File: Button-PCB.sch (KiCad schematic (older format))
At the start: 28 parts

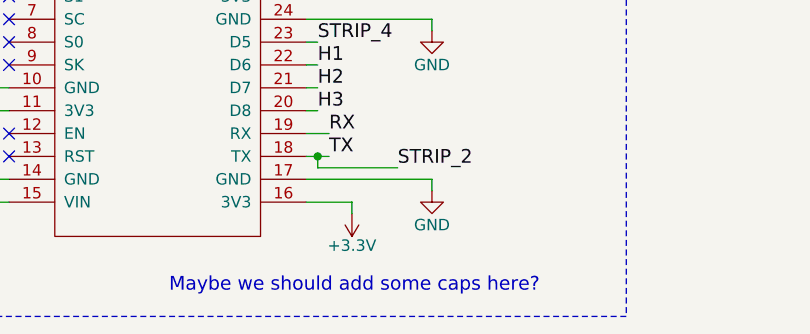
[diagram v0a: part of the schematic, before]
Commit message: Removing note on caps for the nodemcu
Caps are probably not required across the rails of the nodemcu because:

1. The capacitor at the output of the regulator takes care of some
   decoupling already.
2. There's probably a sufficient amount of capacitance on the nodemcu
   board already.
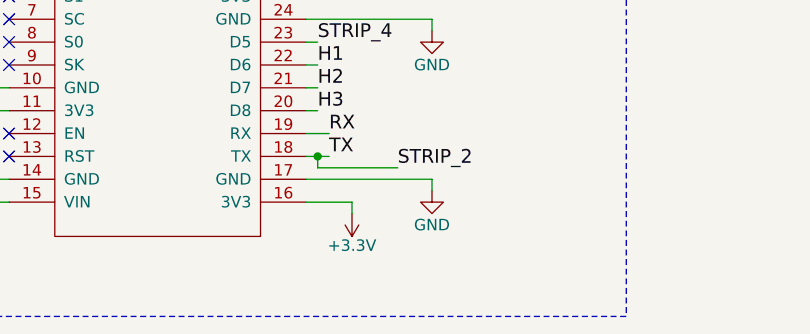
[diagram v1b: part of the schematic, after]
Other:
- note removed: "Maybe we should add some caps here?"
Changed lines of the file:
@@
 LIBS:nodemcuv3
 LIBS:Button-PCB-cache
-EELAYER 25 0
+EELAYER 26 0
 EELAYER END
 $Descr A4 11693 8268
@@
 Wire Wire Line
 	2400 1550 2400 1650
-Text Notes 2900 7000 0    60   ~ 0
-Maybe we should add some caps here?
 Text Notes 600  650  0    60   ~ 0
 Power Input Circuit

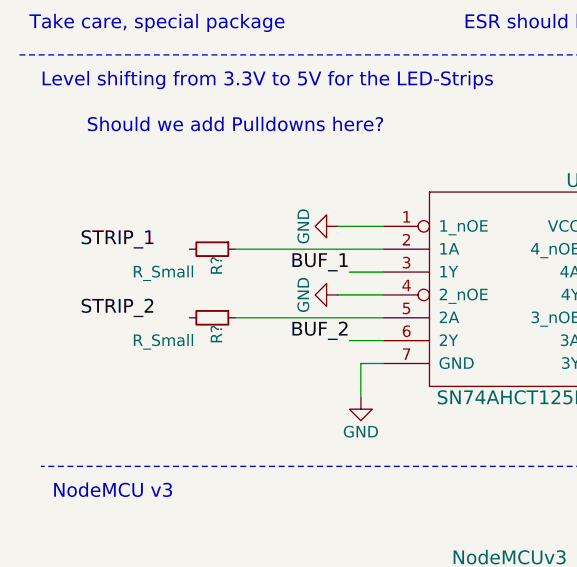
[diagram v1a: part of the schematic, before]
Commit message: Adding missing wire between STRIP label and termination resistors.
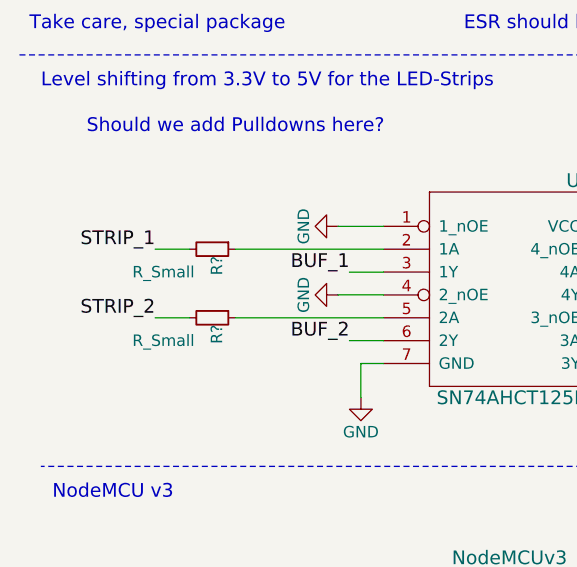
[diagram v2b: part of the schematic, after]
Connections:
- net STRIP_1: now also R?.2
- net STRIP_2: now also R?.2
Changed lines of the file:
@@
 Text Notes 800  3150 0    60   ~ 0
 Should we add Pulldowns here?
+Wire Wire Line
+	1250 3650 1100 3650
+Wire Wire Line
+	1250 3950 1100 3950
 $EndSCHEMATC

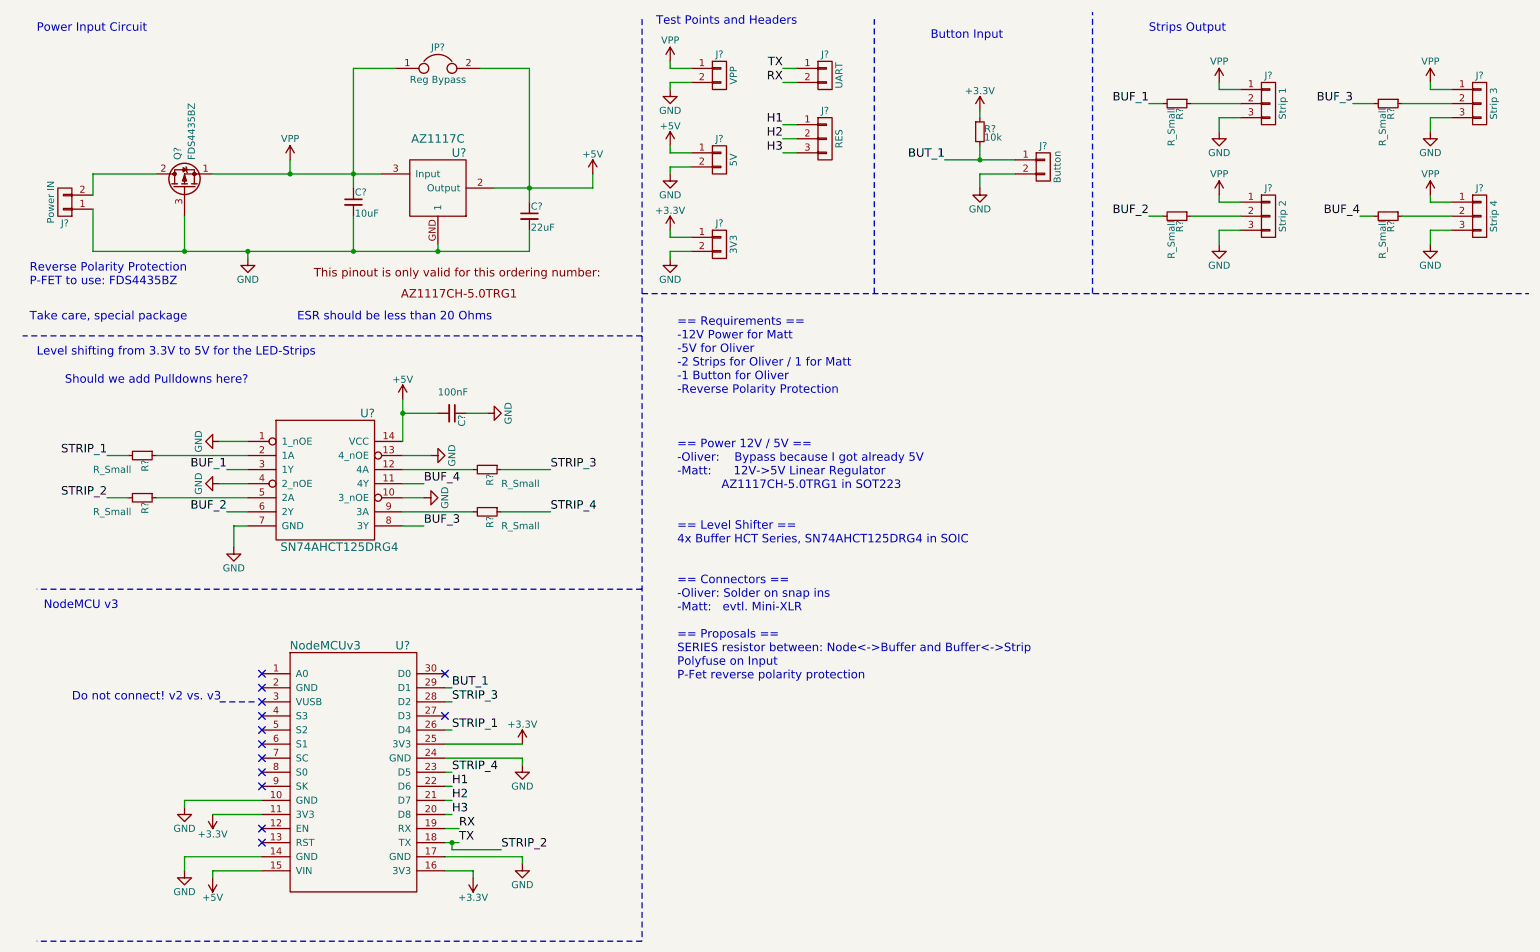
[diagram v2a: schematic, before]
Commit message: Adding 100k pull-down resistors to buffer input.
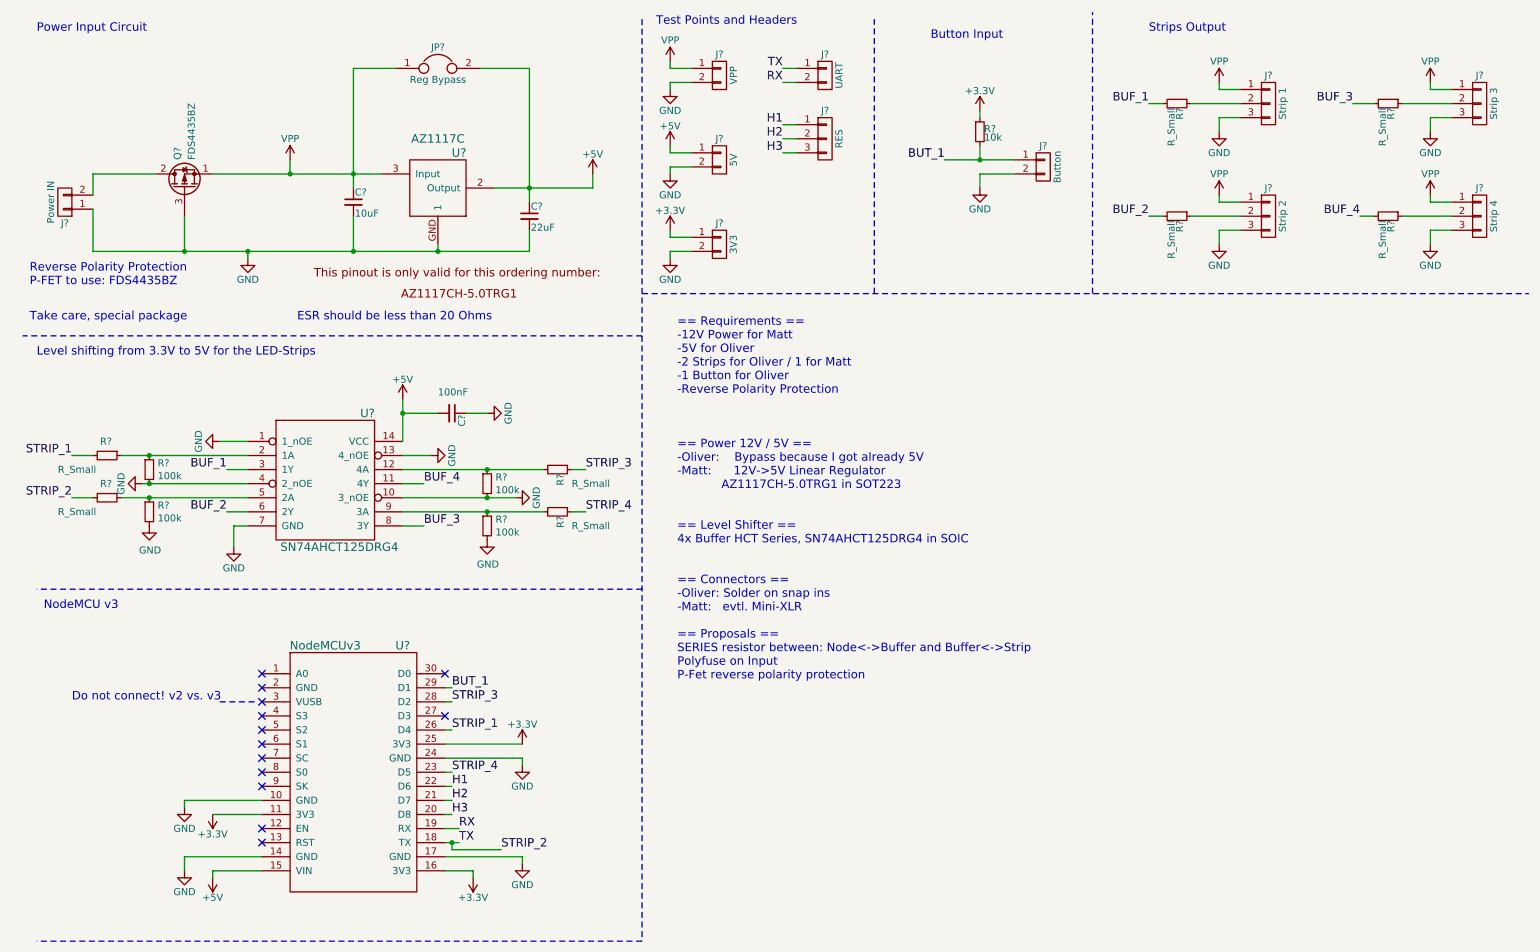
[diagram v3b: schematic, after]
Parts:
- added R? (x4): 100k, symbol R_Small
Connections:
- net GND: now also R?.2, R?.2, R?.2, R?.2
- net at R?.2, U?.12 (4A): now also R?.1
- net at R?.1, U?.2 (1A): now also R?.1
- net at R?.1, U?.5 (2A): now also R?.1
- net at R?.2, U?.9 (3A): now also R?.1
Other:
- note removed: "Should we add Pulldowns here?"
- moved on the sheet: R?
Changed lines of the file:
@@
 	7300 1250 7300 1200
 Wire Wire Line
-	7050 1550 7550 1550
+	7050 1550 7300 1550
+Wire Wire Line
+	7300 1550 7550 1550
 Wire Wire Line
 	7300 1550 7300 1450
@@
 STRIP_2
 Wire Wire Line
-	3500 6400 3600 6400
+	3500 6400 3550 6400
+Wire Wire Line
+	3550 6400 3600 6400
 Wire Wire Line
 	3550 6400 3550 6450
@@
 	3450 2150 3450 2200
 Wire Wire Line
-	3850 1750 4550 1750
+	3850 1750 4100 1750
+Wire Wire Line
+	4100 1750 4550 1750
 Wire Wire Line
 	4550 1750 4550 1650
 Wire Wire Line
-	4100 900  4100 1850
+	4100 900  4100 1750
+Wire Wire Line
+	4100 1750 4100 1850
 Connection ~ 4100 1750
 Wire Wire Line
-	1000 2200 4100 2200
+	1000 2200 1650 2200
+Wire Wire Line
+	1650 2200 2100 2200
+Wire Wire Line
+	2100 2200 2850 2200
+Wire Wire Line
+	2850 2200 3450 2200
+Wire Wire Line
+	3450 2200 4100 2200
 Connection ~ 3450 2200
 Wire Wire Line
@@
 Connection ~ 2850 2200
 Wire Wire Line
-	2850 900  2850 1750
-Wire Wire Line
-	1850 1650 3050 1650
+	2850 900  2850 1650
+Wire Wire Line
+	2850 1650 2850 1750
+Wire Wire Line
+	1850 1650 2400 1650
+Wire Wire Line
+	2400 1650 2850 1650
+Wire Wire Line
+	2850 1650 3050 1650
 $Comp
 L Jumper JP?
@@
 L GND #PWR?
 U 1 1 5942C499
-P 3350 3950
-F 0 "#PWR?" H 3350 3700 50  0001 C CNN
-F 1 "GND" H 3350 3800 50  0000 C CNN
-F 2 "" H 3350 3950 50  0001 C CNN
-F 3 "" H 3350 3950 50  0001 C CNN
-	1    3350 3950
+P 4000 3950
+F 0 "#PWR?" H 4000 3700 50  0001 C CNN
+F 1 "GND" H 4000 3800 50  0000 C CNN
+F 2 "" H 4000 3950 50  0001 C CNN
+F 3 "" H 4000 3950 50  0001 C CNN
+	1    4000 3950
 	0    -1   -1   0
 $EndComp
-Text Label 1100 3950 2    60   ~ 0
+Text Label 850  3950 2    60   ~ 0
 STRIP_2
-Text Label 1100 3650 2    60   ~ 0
+Text Label 850  3650 2    60   ~ 0
 STRIP_1
-Text Label 4250 3750 0    60   ~ 0
+Text Label 4500 3750 0    60   ~ 0
 STRIP_3
-Text Label 4250 4050 0    60   ~ 0
+Text Label 4500 4050 0    60   ~ 0
 STRIP_4
 $Comp
 L R_Small R?
 U 1 1 5942C75E
-P 1350 3650
-F 0 "R?" H 1380 3670 50  0000 L CNN
-F 1 "R_Small" V 1450 3300 50  0000 L CNN
-F 2 "" H 1350 3650 50  0001 C CNN
-F 3 "" H 1350 3650 50  0001 C CNN
-	1    1350 3650
+P 1100 3650
+F 0 "R?" V 1000 3600 50  0000 L CNN
+F 1 "R_Small" V 1200 3300 50  0000 L CNN
+F 2 "" H 1100 3650 50  0001 C CNN
+F 3 "" H 1100 3650 50  0001 C CNN
+	1    1100 3650
 	0    1    1    0
 $EndComp
@@
 L R_Small R?
 U 1 1 5942CA98
-P 1350 3950
-F 0 "R?" H 1380 3970 50  0000 L CNN
-F 1 "R_Small" V 1450 3600 50  0000 L CNN
-F 2 "" H 1350 3950 50  0001 C CNN
-F 3 "" H 1350 3950 50  0001 C CNN
-	1    1350 3950
+P 1100 3950
+F 0 "R?" V 1000 3900 50  0000 L CNN
+F 1 "R_Small" V 1200 3600 50  0000 L CNN
+F 2 "" H 1100 3950 50  0001 C CNN
+F 3 "" H 1100 3950 50  0001 C CNN
+	1    1100 3950
 	0    1    1    0
 $EndComp
@@
 	1950 3750 2100 3750
 Wire Wire Line
-	1450 3650 2100 3650
-Wire Wire Line
-	1450 3950 2100 3950
+	1200 3650 1400 3650
+Wire Wire Line
+	1400 3650 2100 3650
+Wire Wire Line
+	1200 3950 1400 3950
+Wire Wire Line
+	1400 3950 2100 3950
 $Comp
 L GND #PWR?
 U 1 1 5942E71C
-P 1900 3850
-F 0 "#PWR?" H 1900 3600 50  0001 C CNN
-F 1 "GND" H 1900 3700 50  0000 C CNN
-F 2 "" H 1900 3850 50  0001 C CNN
-F 3 "" H 1900 3850 50  0001 C CNN
-	1    1900 3850
+P 1350 3850
+F 0 "#PWR?" H 1350 3600 50  0001 C CNN
+F 1 "GND" H 1350 3700 50  0000 C CNN
+F 2 "" H 1350 3850 50  0001 C CNN
+F 3 "" H 1350 3850 50  0001 C CNN
+	1    1350 3850
 	0    1    1    0
 $EndComp
 Wire Wire Line
-	1900 3850 2100 3850
+	1350 3850 1400 3850
+Wire Wire Line
+	1400 3850 2100 3850
 $Comp
 L GND #PWR?
@@
 	1900 3550 2100 3550
 Wire Wire Line
-	3350 3950 3200 3950
+	4000 3950 3800 3950
+Wire Wire Line
+	3800 3950 3200 3950
 Wire Wire Line
 	3400 3650 3200 3650
@@
 L R_Small R?
 U 1 1 5942EF55
-P 3800 3750
-F 0 "R?" H 3830 3770 50  0000 L CNN
-F 1 "R_Small" V 3900 3850 50  0000 L CNN
-F 2 "" H 3800 3750 50  0001 C CNN
-F 3 "" H 3800 3750 50  0001 C CNN
-	1    3800 3750
+P 4300 3750
+F 0 "R?" H 4330 3770 50  0000 L CNN
+F 1 "R_Small" V 4400 3850 50  0000 L CNN
+F 2 "" H 4300 3750 50  0001 C CNN
+F 3 "" H 4300 3750 50  0001 C CNN
+	1    4300 3750
 	0    1    1    0
 $EndComp
@@
 L R_Small R?
 U 1 1 5942F05B
-P 3800 4050
-F 0 "R?" H 3830 4070 50  0000 L CNN
-F 1 "R_Small" V 3900 4150 50  0000 L CNN
-F 2 "" H 3800 4050 50  0001 C CNN
-F 3 "" H 3800 4050 50  0001 C CNN
-	1    3800 4050
+P 4300 4050
+F 0 "R?" H 4330 4070 50  0000 L CNN
+F 1 "R_Small" V 4400 4150 50  0000 L CNN
+F 2 "" H 4300 4050 50  0001 C CNN
+F 3 "" H 4300 4050 50  0001 C CNN
+	1    4300 4050
 	0    1    1    0
 $EndComp
 Wire Wire Line
-	3200 3750 3700 3750
-Wire Wire Line
-	3200 4050 3700 4050
-Wire Wire Line
-	3900 3750 4250 3750
-Wire Wire Line
-	4250 4050 3900 4050
+	3200 3750 3800 3750
+Wire Wire Line
+	3800 3750 4200 3750
+Wire Wire Line
+	3200 4050 3800 4050
+Wire Wire Line
+	3800 4050 4200 4050
+Wire Wire Line
+	4400 3750 4500 3750
+Wire Wire Line
+	4500 4050 4400 4050
 $Comp
 L C_Small C?
@@
 	3450 3350 3200 3350
 Wire Wire Line
-	3200 3250 3200 3550
+	3200 3250 3200 3350
+Wire Wire Line
+	3200 3350 3200 3550
 $Comp
 L +5V #PWR?
@@
 Wire Notes Line
 	4900 7100 600  7100
-Text Notes 800  3150 0    60   ~ 0
-Should we add Pulldowns here?
-Wire Wire Line
-	1250 3650 1100 3650
-Wire Wire Line
-	1250 3950 1100 3950
+Wire Wire Line
+	1000 3650 850  3650
+Wire Wire Line
+	1000 3950 850  3950
+$Comp
+L R_Small R?
+U 1 1 5945C430
+P 1400 4050
+F 0 "R?" H 1459 4096 50  0000 L CNN
+F 1 "100k" H 1459 4005 50  0000 L CNN
+F 2 "" H 1400 4050 50  0001 C CNN
+F 3 "" H 1400 4050 50  0001 C CNN
+	1    1400 4050
+	1    0    0    -1
+$EndComp
+$Comp
+L R_Small R?
+U 1 1 5945C4B9
+P 1400 3750
+F 0 "R?" H 1459 3796 50  0000 L CNN
+F 1 "100k" H 1459 3705 50  0000 L CNN
+F 2 "" H 1400 3750 50  0001 C CNN
+F 3 "" H 1400 3750 50  0001 C CNN
+	1    1400 3750
+	1    0    0    -1
+$EndComp
+$Comp
+L R_Small R?
+U 1 1 5945C541
+P 3800 3850
+F 0 "R?" H 3859 3896 50  0000 L CNN
+F 1 "100k" H 3859 3805 50  0000 L CNN
+F 2 "" H 3800 3850 50  0001 C CNN
+F 3 "" H 3800 3850 50  0001 C CNN
+	1    3800 3850
+	1    0    0    -1
+$EndComp
+$Comp
+L R_Small R?
+U 1 1 5945C5D0
+P 3800 4150
+F 0 "R?" H 3859 4196 50  0000 L CNN
+F 1 "100k" H 3859 4105 50  0000 L CNN
+F 2 "" H 3800 4150 50  0001 C CNN
+F 3 "" H 3800 4150 50  0001 C CNN
+	1    3800 4150
+	1    0    0    -1
+$EndComp
+Connection ~ 3800 3750
+Connection ~ 3800 4050
+Connection ~ 1400 3650
+Connection ~ 1400 3950
+Connection ~ 1400 3850
+$Comp
+L GND #PWR?
+U 1 1 5945C779
+P 1400 4150
+F 0 "#PWR?" H 1400 3900 50  0001 C CNN
+F 1 "GND" H 1405 3977 50  0000 C CNN
+F 2 "" H 1400 4150 50  0001 C CNN
+F 3 "" H 1400 4150 50  0001 C CNN
+	1    1400 4150
+	1    0    0    -1
+$EndComp
+$Comp
+L GND #PWR?
+U 1 1 5945C810
+P 3800 4250
+F 0 "#PWR?" H 3800 4000 50  0001 C CNN
+F 1 "GND" H 3805 4077 50  0000 C CNN
+F 2 "" H 3800 4250 50  0001 C CNN
+F 3 "" H 3800 4250 50  0001 C CNN
+	1    3800 4250
+	1    0    0    -1
+$EndComp
+Connection ~ 3800 3950
 $EndSCHEMATC
